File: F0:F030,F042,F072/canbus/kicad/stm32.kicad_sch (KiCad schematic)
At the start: 61 parts

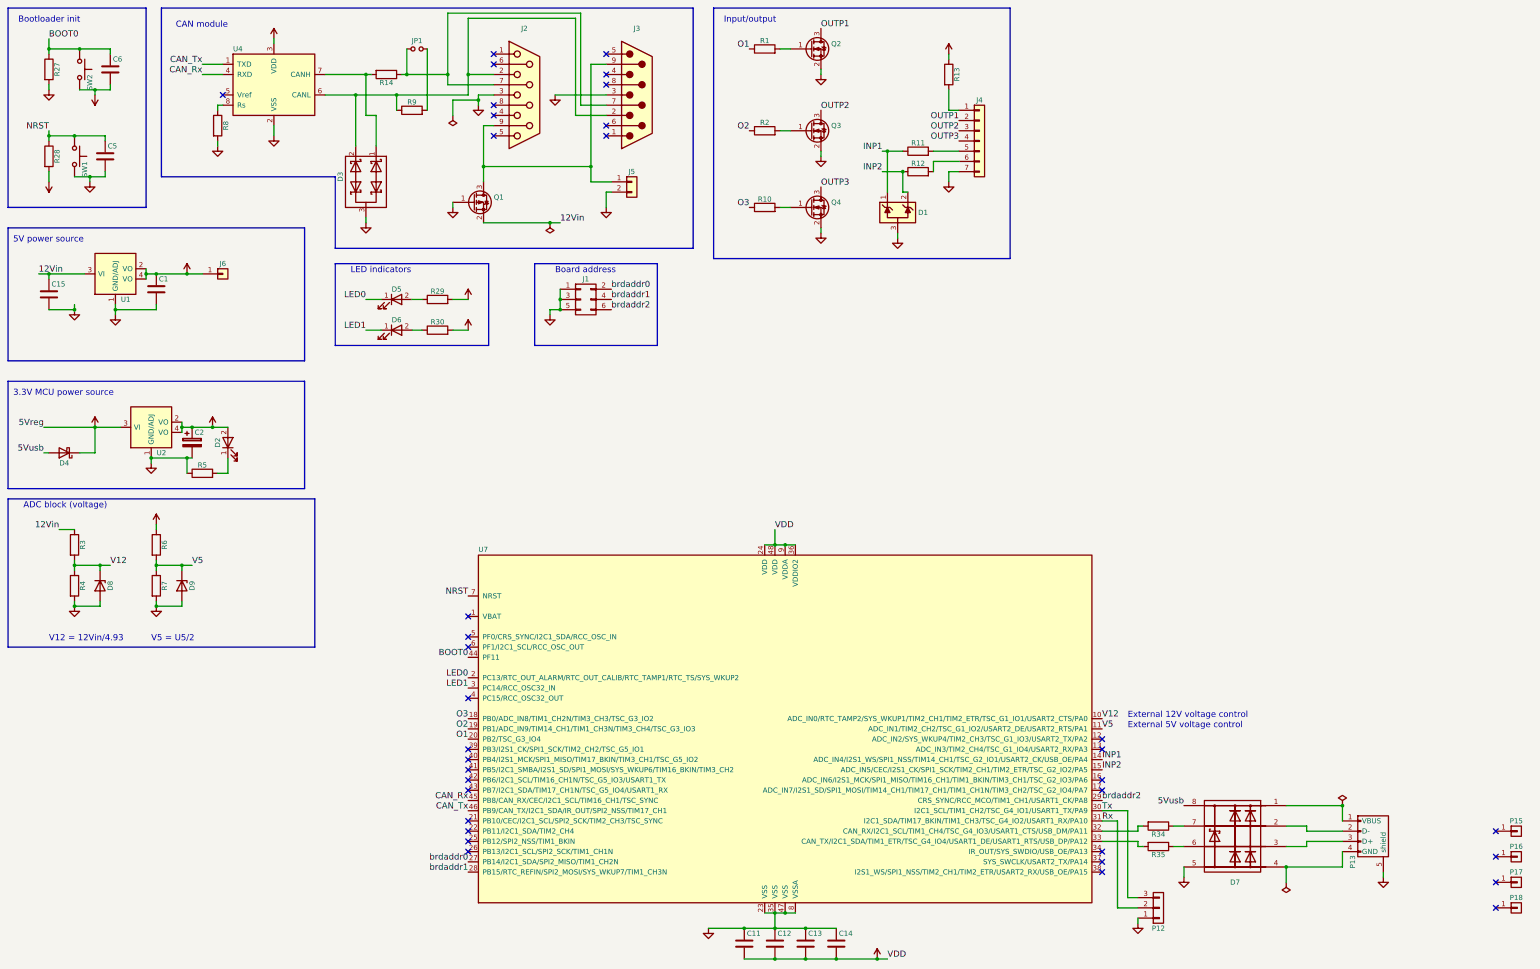
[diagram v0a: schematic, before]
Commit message: -> kicad 8
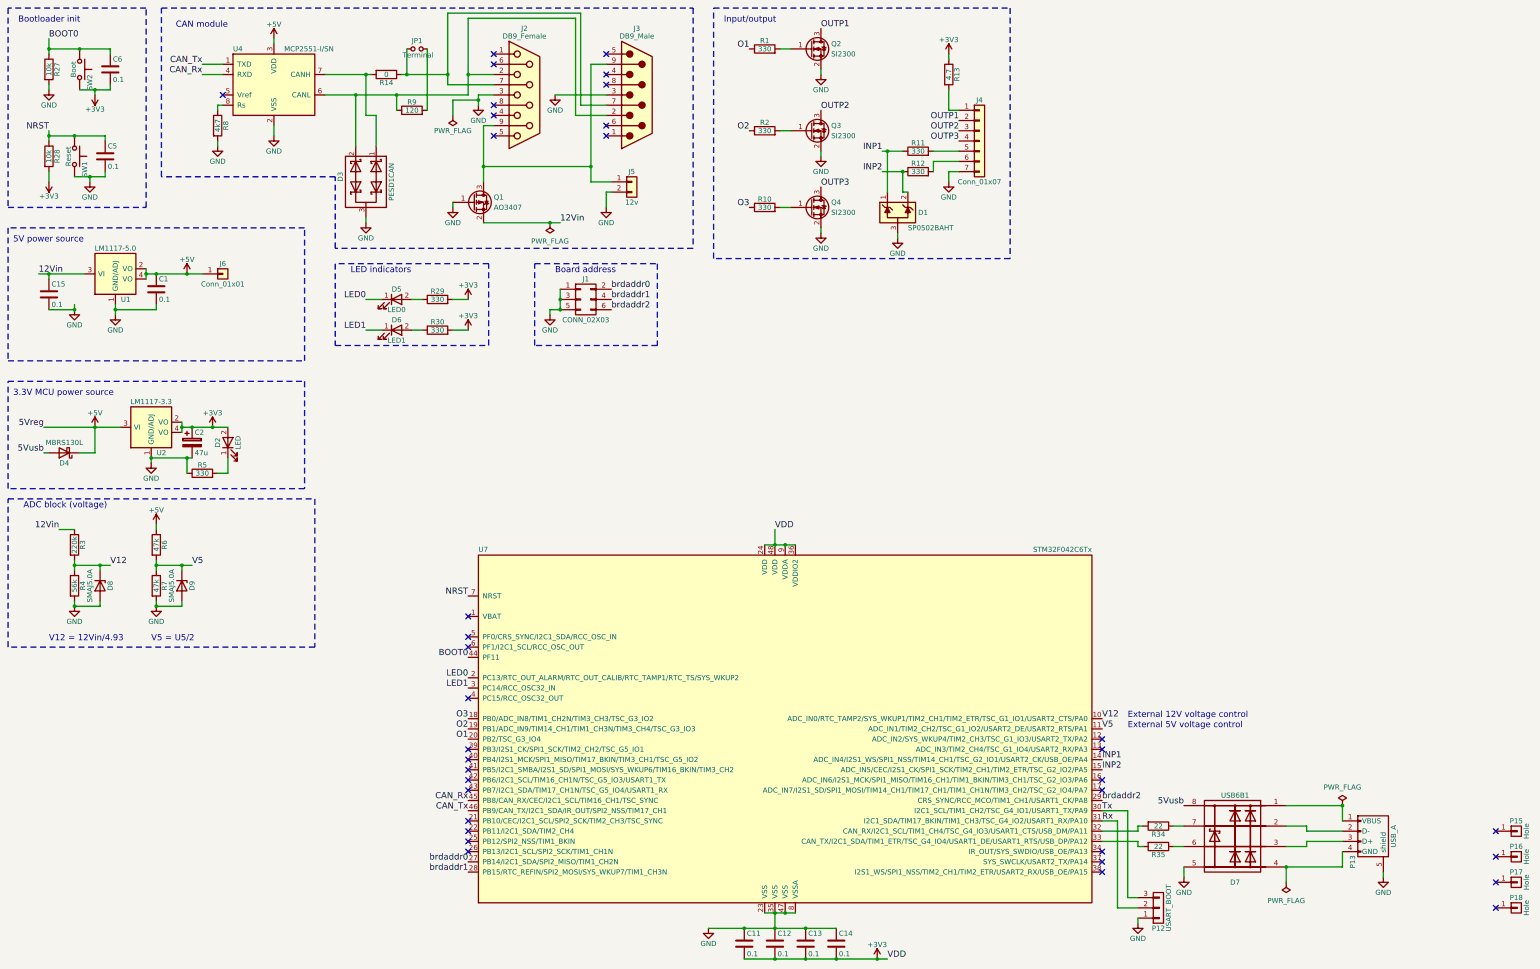
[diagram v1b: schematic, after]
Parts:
- C1, C11, C12, C13, C14, C15, C5, C6: value (none) -> 0.1; footprint (none) -> Capacitors_SMD.pretty:C_0603_HandSoldering
- C2: value (none) -> 47u; footprint (none) -> Capacitors_Tantalum_SMD.pretty:Tantalum_Case-A_EIA-3216-18_Hand
- D1: value (none) -> SP0502BAHT; footprint (none) -> TO_SOT_Packages_SMD.pretty:SOT-23
- D2: value (none) -> LED; footprint (none) -> LEDs.pretty:LED_0805
- D3: value (none) -> PESD1CAN; footprint (none) -> TO_SOT_Packages_SMD.pretty:SOT-23
- D4: value (none) -> MBRS130L; footprint (none) -> Diodes_SMD.pretty:D_SMB_Handsoldering
- D5: value (none) -> LED0; footprint (none) -> LEDs.pretty:LED_0805
- D6: value (none) -> LED1; footprint (none) -> LEDs.pretty:LED_0805
- D7: value (none) -> USB6B1; footprint (none) -> Housings_SOIC.pretty:SOIC-8_3.9x4.9mm_Pitch1.27mm
- D8, D9: value (none) -> SMAJ5.0A; footprint (none) -> Diode_SMD.pretty:D_SMA
- J1: value (none) -> CONN_02X03; footprint (none) -> Pin_Headers.pretty:Pin_Header_Straight_2x03_Pitch2.54mm
- J2: value (none) -> DB9_Female; footprint (none) -> Connectors.pretty:DB9FC
- J3: value (none) -> DB9_Male; footprint (none) -> Connectors.pretty:DB9MC
- J4: value (none) -> Conn_01x07; footprint (none) -> Pin_Headers.pretty:Pin_Header_Straight_1x07_Pitch2.54mm
- J5: value (none) -> 12v; footprint (none) -> Connectors_Terminal_Blocks.pretty:TerminalBlock_Pheonix_MKDS1.5-2pol
- J6: value (none) -> Conn_01x01; footprint (none) -> Pin_Headers.pretty:Pin_Header_Straight_1x01_Pitch2.54mm
- JP1: value (none) -> Terminal; footprint (none) -> Pin_Headers.pretty:Pin_Header_Straight_1x02
- P12: value (none) -> USART_BOOT; footprint (none) -> Pin_Headers.pretty:Pin_Header_Straight_1x03
- P13: value (none) -> USB_A; footprint (none) -> Connect.pretty:USB_Mini-B
- P15, P16, P17, P18: value (none) -> Hole; footprint (none) -> my_footprints:Hole_3mm
- Q1: value (none) -> AO3407; footprint (none) -> TO_SOT_Packages_SMD.pretty:SOT-23_Handsoldering
- Q2, Q3, Q4: value (none) -> SI2300; footprint (none) -> TO_SOT_Packages_SMD.pretty:SOT-23_Handsoldering
- R1, R10, R11, R12, R2, R29, R30, R5: value (none) -> 330; footprint (none) -> Resistors_SMD.pretty:R_0603_HandSoldering
- R13: value (none) -> 4.7; footprint (none) -> Resistors_SMD.pretty:R_0603_HandSoldering
- R14: value (none) -> 0; footprint (none) -> Resistors_SMD.pretty:R_0805_HandSoldering
- R27, R28: value (none) -> 10k; footprint (none) -> Resistors_SMD.pretty:R_0603_HandSoldering
- R3: value (none) -> 220k; footprint (none) -> Resistors_SMD.pretty:R_0603_HandSoldering
- R34, R35: value (none) -> 22; footprint (none) -> Resistors_SMD.pretty:R_0603_HandSoldering
- R4: value (none) -> 56k; footprint (none) -> Resistors_SMD.pretty:R_0603_HandSoldering
- R6, R7: value (none) -> 47k; footprint (none) -> Resistors_SMD.pretty:R_0603_HandSoldering
- R8: value (none) -> 4k7; footprint (none) -> Resistors_SMD.pretty:R_0603_HandSoldering
- R9: value (none) -> 120; footprint (none) -> Resistors_SMD.pretty:R_0603_HandSoldering
- SW1: value (none) -> Reset; footprint (none) -> Buttons_Switches_SMD.pretty:SW_SPST_FSMSM
- SW2: value (none) -> Boot; footprint (none) -> Buttons_Switches_SMD.pretty:SW_SPST_FSMSM
- U1: value (none) -> LM1117-5.0; footprint (none) -> TO_SOT_Packages_SMD.pretty:SOT-223
- U2: value (none) -> LM1117-3.3; footprint (none) -> TO_SOT_Packages_SMD.pretty:SOT-223
- U4: value (none) -> MCP2551-I/SN; footprint (none) -> Housings_SOIC.pretty:SOIC-8_3.9x4.9mm_Pitch1.27mm
- U7: value (none) -> STM32F042C6Tx; footprint (none) -> Housings_QFP.pretty:LQFP-48_7x7mm_Pitch0.5mm
